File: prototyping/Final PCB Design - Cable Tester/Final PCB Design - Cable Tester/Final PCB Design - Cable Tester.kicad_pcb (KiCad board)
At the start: 2 copper layers, 86 x 54 mm, 41 parts, among them J17 Banana Jack, J20 SFML-110-02-L-D-A, J3 Debug Connection, J4 MicroSD, J5 Barrel Jack 9V, J6 Touchscreen HMI, Q1 2N3904, SW1 Rocker Switch, U1 AVR128DB64x-xMR, U2 LP2985-3.3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

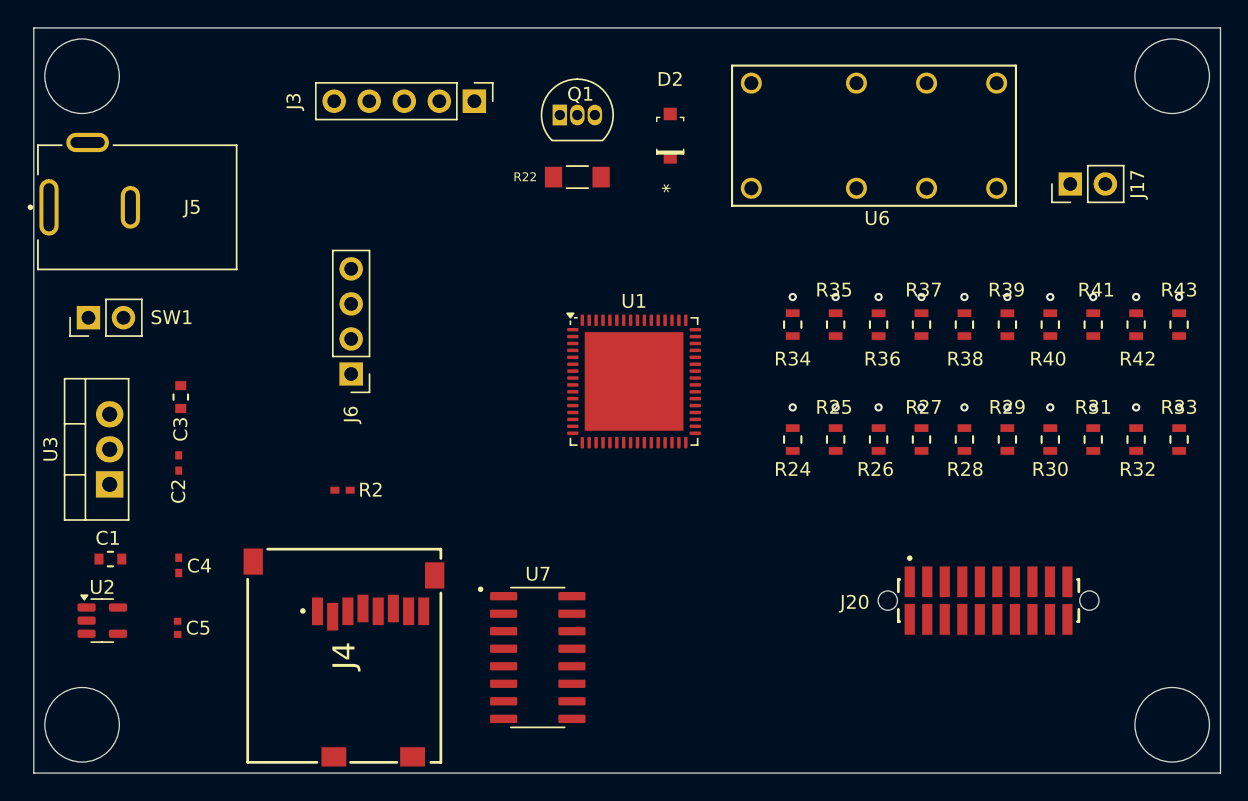
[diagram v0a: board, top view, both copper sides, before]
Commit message: Laying out final PCB.
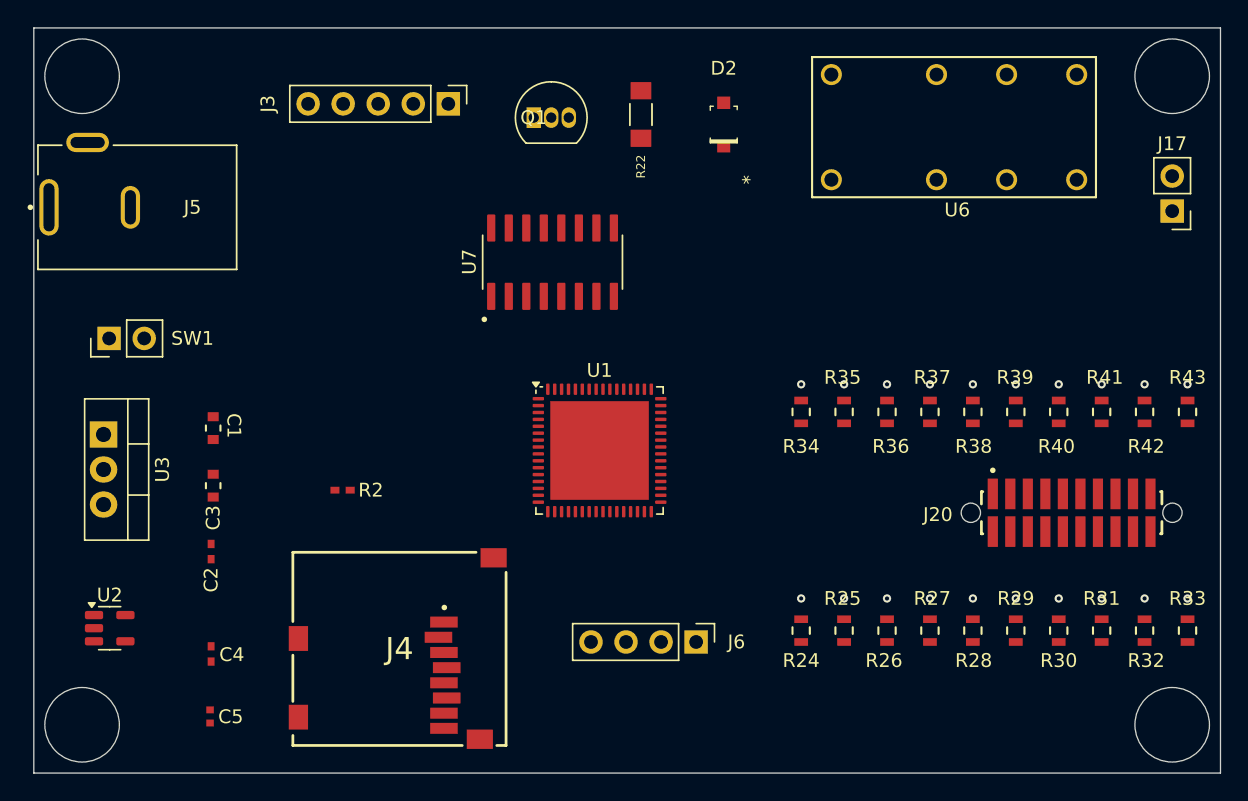
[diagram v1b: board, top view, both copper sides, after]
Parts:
- moved J6 31.7 mm to (139.5, 110.5), turned to -90 degrees
- moved U7 28.7 mm to (129.1, 83.0), turned to 90 degrees
- moved R24 13.9 mm to (147.1, 109.7)
- moved R25 13.9 mm to (150.2, 109.7)
- moved R26 13.9 mm to (153.3, 109.7)
- moved R27 13.9 mm to (156.4, 109.7)
- moved R28 13.9 mm to (159.6, 109.7)
- moved R29 13.9 mm to (162.7, 109.7)
- moved R30 13.9 mm to (165.8, 109.7)
- moved R31 13.9 mm to (168.9, 109.7)
- moved R32 13.9 mm to (172.0, 109.7)
- moved R33 13.9 mm to (175.1, 109.7)
- moved C1 12.1 mm to (104.5, 95.0), turned to -90 degrees
- moved J20 8.76 mm to (166.7, 101.1)
- moved J17 7.64 mm to (174.0, 79.3), turned to 180 degrees
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
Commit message: Updated.
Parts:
- moved U7 9.75 mm to (119.5, 81.1), turned to 180 degrees
- moved U1 2.85 mm to (135.1, 95.5)
- moved C1 1.00 mm to (104.5, 94.0), turned to 90 degrees

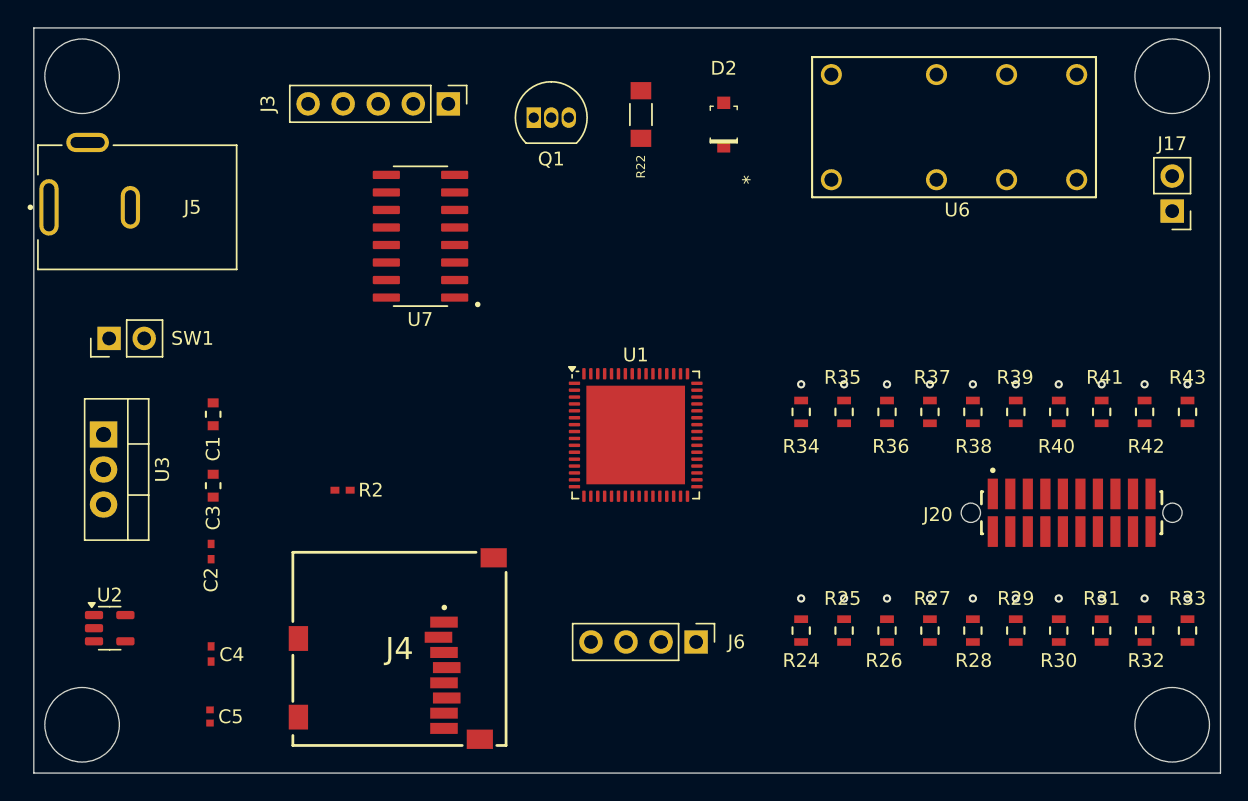
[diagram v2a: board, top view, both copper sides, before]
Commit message: Updates to final PCB
Final PCB design updates - placed traces and vias to Analog IF circuit and changed order of analog pins 1-10 on schematic and PCB layout.
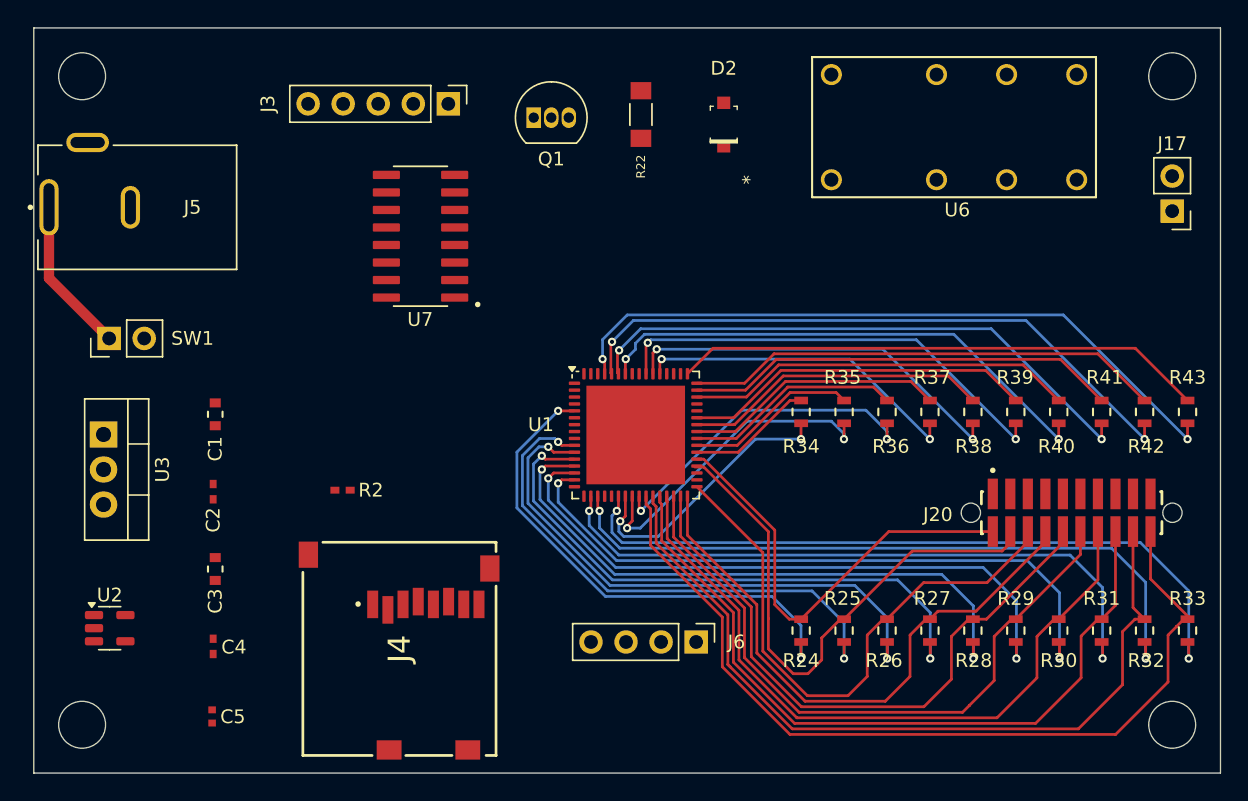
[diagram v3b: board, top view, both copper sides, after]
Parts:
- J4: value MicroSD -> MEM2061-01-188-00-A_REVA
- moved C3 6.04 mm to (104.7, 105.2)
- moved C2 4.34 mm to (104.5, 99.6)
- moved C4 0.57 mm to (104.5, 110.8)
- moved C1 0.15 mm to (104.7, 94.0)
- moved C5 0.15 mm to (104.4, 115.9)
- turned J4 to 180 degrees
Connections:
- C1 pad 2: CD -> GND
- C2 pad 2: CD -> GND
- C3 pad 2: CD -> GND
- C4 pad 2: CD -> GND
- C5 pad 2: CD -> GND
- J3 pad 1: CD -> GND
- J4 pad 11: CD -> GND
- J4 pad 12: CD -> GND
- J4 pad 2: CD -> /mSD_CS
- J4 pad 3: CD -> /mSD_DI
- J4 pad 5: CD -> /mSD_CLK
- J4 pad 6: CD -> GND
- J4 pad 7: CD -> /mSD_DO
- J5 pad B: CD -> GND
- J5 pad C: CD -> GND
- J6 pad 4: CD -> GND
- Q1 pad 1: CD -> GND
- U1 pad 21: CD -> GND
- U1 pad 26: ADC 1 -> ADC 10
- U1 pad 27: ADC 2 -> ADC 9
- U1 pad 28: ADC 3 -> ADC 8
- U1 pad 29: ADC 4 -> ADC 7
- U1 pad 30: ADC 5 -> ADC 6
- U1 pad 31: ADC 6 -> ADC 5
- U1 pad 32: ADC 7 -> ADC 4
- U1 pad 33: ADC 8 -> ADC 3
- U1 pad 35: CD -> GND
- U1 pad 36: ADC 9 -> ADC 2
- U1 pad 37: ADC 10 -> ADC 1
- U1 pad 57: CD -> GND
- U1 pad 65: CD -> GND
- U1 pad 7: CD -> GND
- U2 pad 2: CD -> GND
- U3 pad 2: CD -> GND
- U6 pad 4: CD -> GND
- U7 pad 10: CD -> /mSD_CLK
- U7 pad 11: CD -> GND
- U7 pad 14: CD -> GND
- U7 pad 2: CD -> /mSD_DO
- U7 pad 4: CD -> /mSD_CS
- U7 pad 6: CD -> /mSD_DI
- U7 pad 8: CD -> GND
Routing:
- net ADC 10: track 0.00 -> 63.3 mm
- net ADC 9: track 0.00 -> 59.1 mm
- net ADC 8: track 0.00 -> 54.4 mm
- net CTRL 10: track 0.00 -> 52.5 mm, vias 0 -> 2
- net ADC 7: track 0.00 -> 51.2 mm
- net CTRL 20: track 0.00 -> 50.5 mm, vias 0 -> 2
- net CTRL 9: track 0.00 -> 50.3 mm, vias 0 -> 2
- net ADC 6: track 0.00 -> 48.1 mm
- net CTRL 7: track 0.00 -> 47.7 mm, vias 0 -> 2
- net CTRL 8: track 0.00 -> 47.6 mm, vias 0 -> 2
- net CTRL 19: track 0.00 -> 46.3 mm, vias 0 -> 2
- net CTRL 6: track 0.00 -> 46.0 mm, vias 0 -> 2
- net ADC 5: track 0.00 -> 45.4 mm
- net CTRL 5: track 0.00 -> 44.3 mm, vias 0 -> 2
- net ADC 4: track 0.00 -> 43.1 mm
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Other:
- outline, holes or cut-outs redrawn

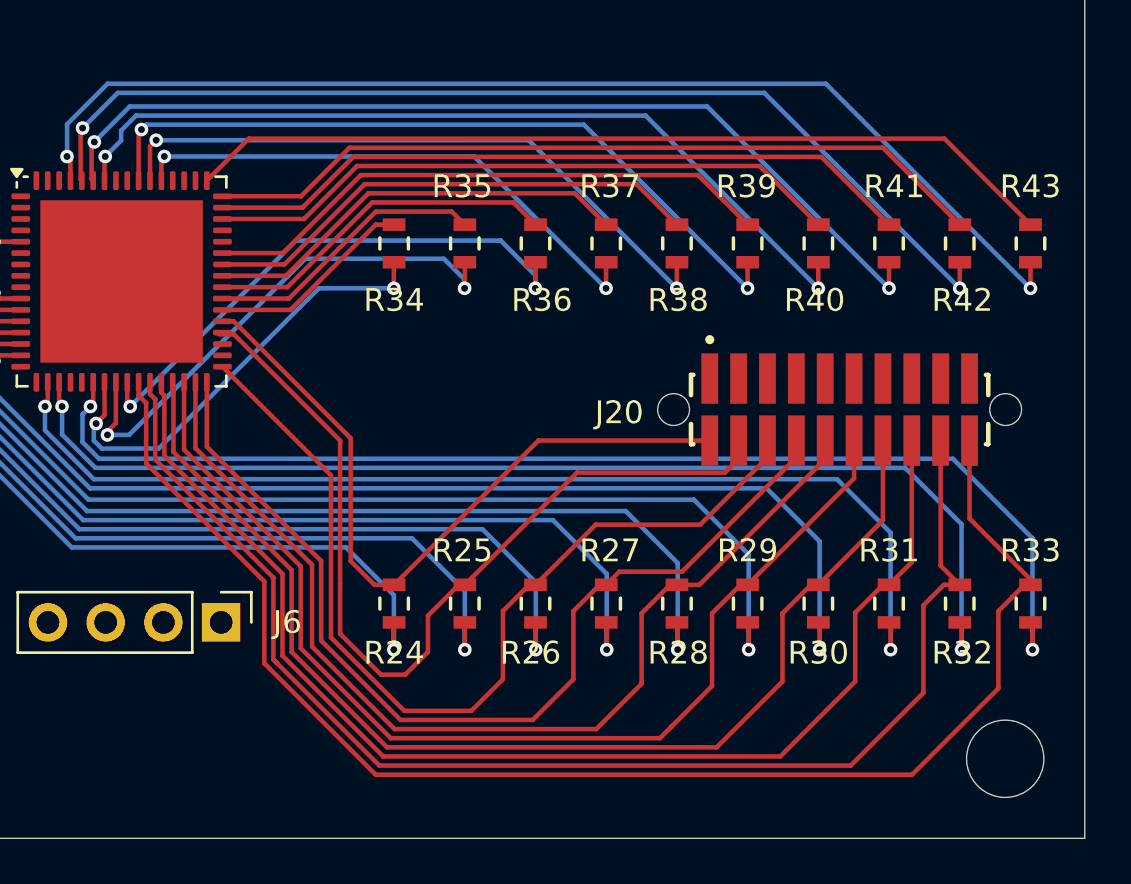
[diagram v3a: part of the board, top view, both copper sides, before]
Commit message: Updated Final PCB Layout
Refined some of the ADC trace layouts. Less sharp corners and smoother traces
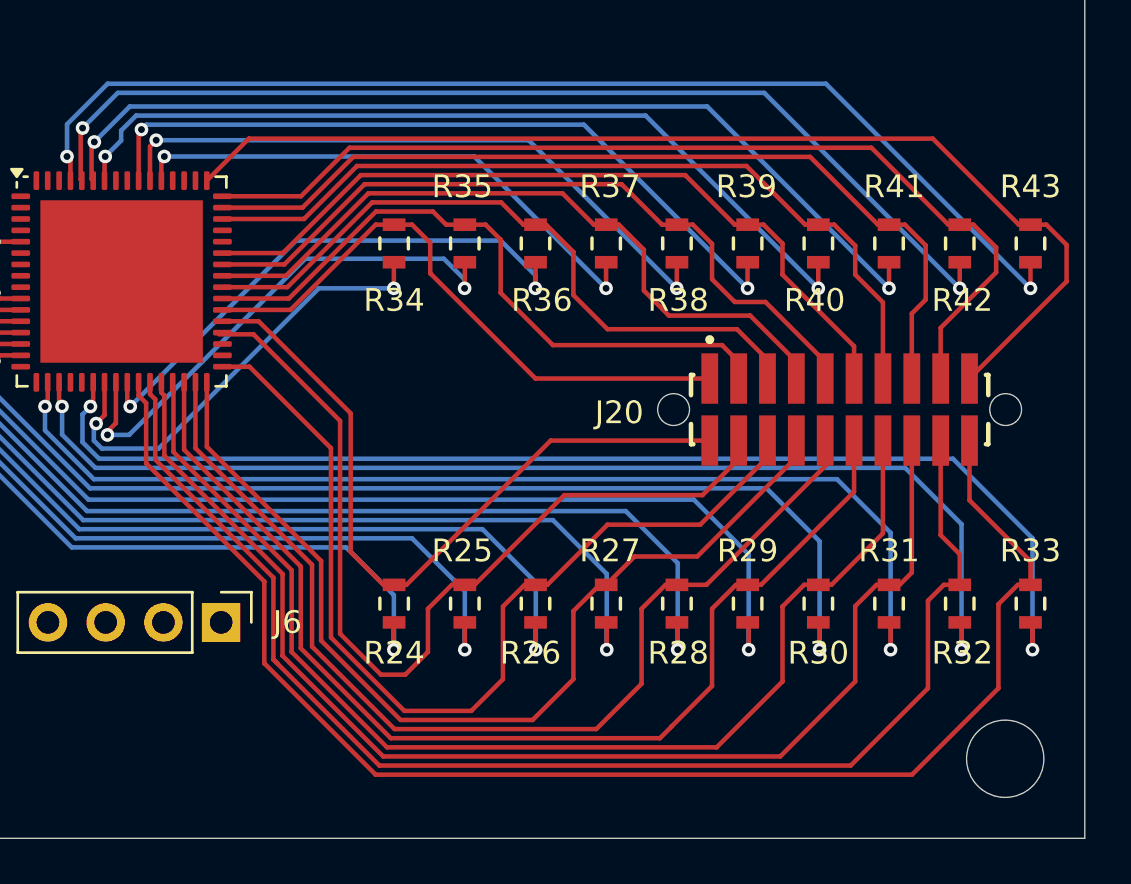
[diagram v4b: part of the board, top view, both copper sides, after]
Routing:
- net ADC 11: track 9.11 -> 26.6 mm
- net ADC 12: track 12.5 -> 29.1 mm
- net ADC 13: track 15.7 -> 30.3 mm
- net ADC 14: track 19.0 -> 31.6 mm
- net ADC 15: track 22.2 -> 32.9 mm
- net ADC 20: track 38.6 -> 48.2 mm
- net ADC 16: track 25.4 -> 34.6 mm
- net ADC 19: track 34.7 -> 43.5 mm
- net ADC 17: track 28.3 -> 36.6 mm
- net ADC 18: track 31.5 -> 39.6 mm
- net ADC 3: track 41.6 -> 42.4 mm
- net ADC 2: track 39.7 -> 40.4 mm
- net ADC 7: track 51.2 -> 51.7 mm

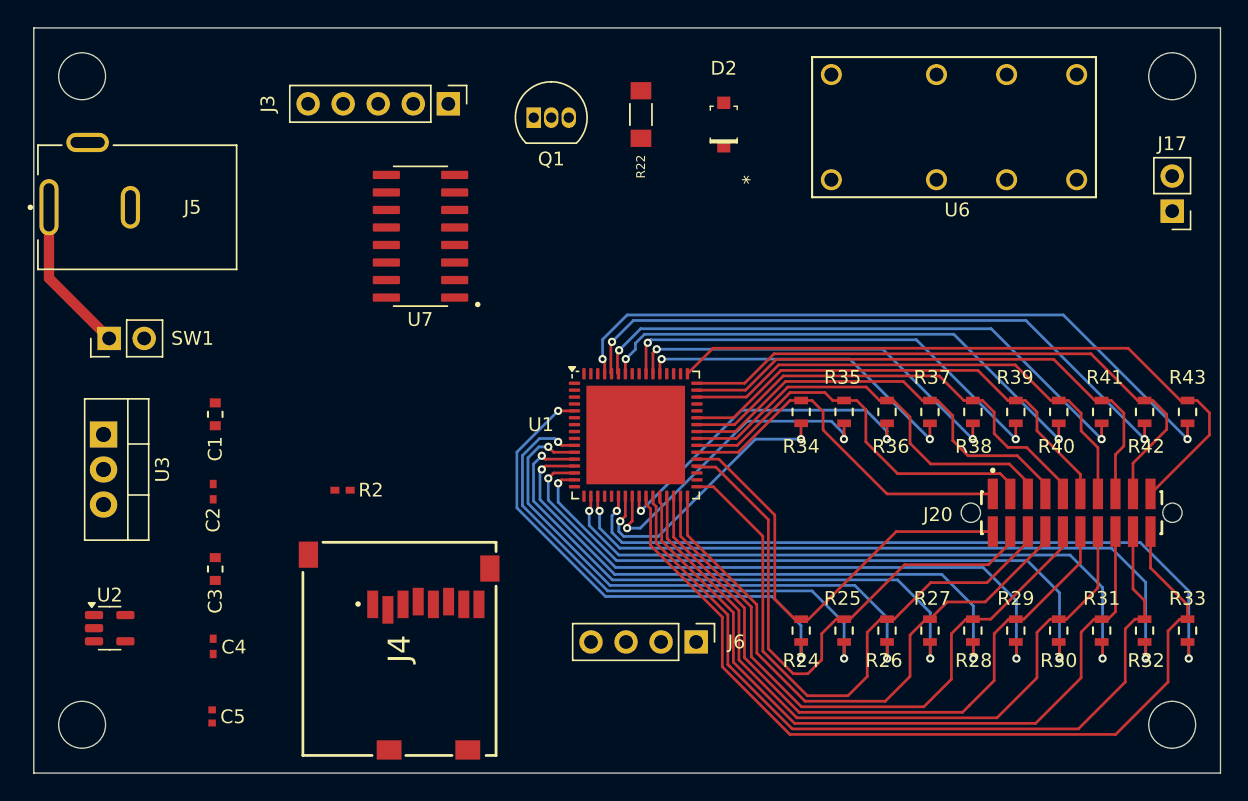
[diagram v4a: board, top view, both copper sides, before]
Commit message: updated prototype PCB layout
Fixed backwards barrel jack and made small minor changes to silkscreen layer so that paint is not overlapping solder points.
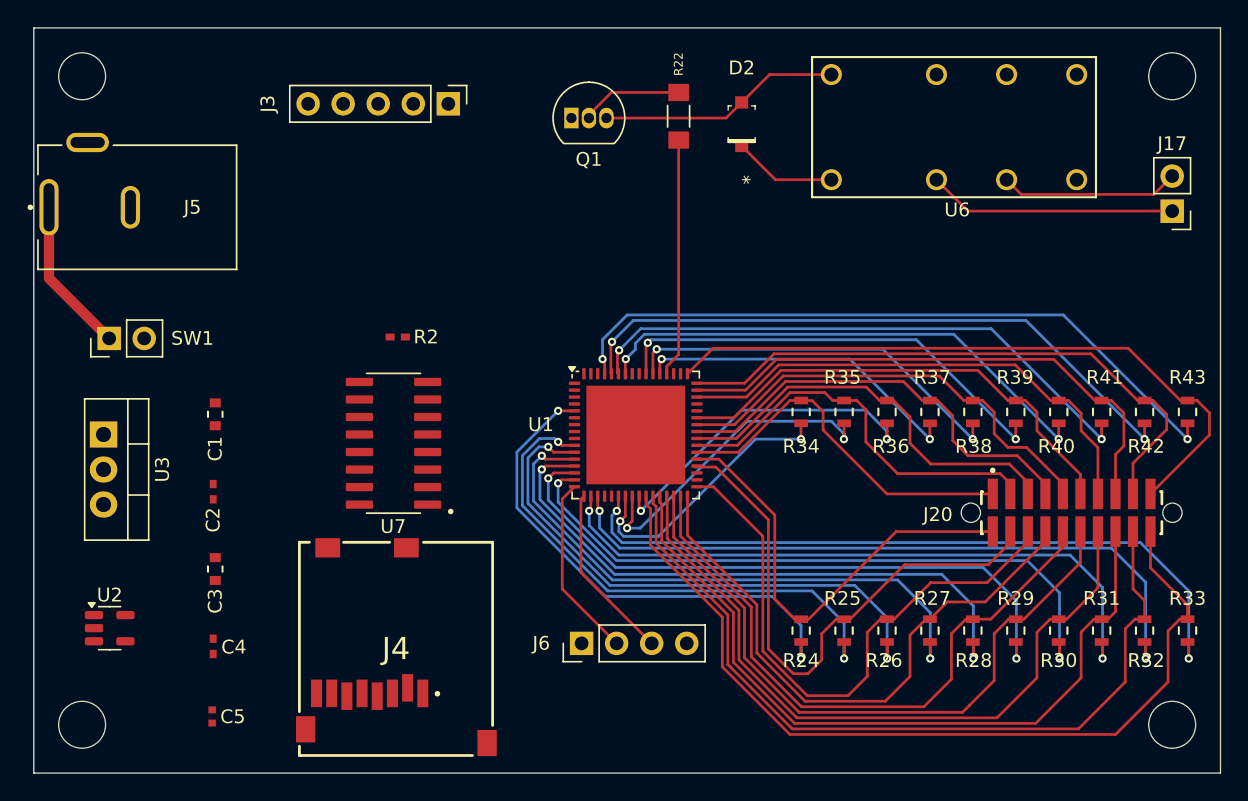
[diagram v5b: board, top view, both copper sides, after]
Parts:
- moved U7 15.1 mm to (117.6, 96.1)
- moved R2 11.8 mm to (117.9, 88.4)
- moved J6 8.30 mm to (131.2, 110.6), turned to 90 degrees
- moved R22 2.73 mm to (138.2, 72.4), turned to 90 degrees
- moved Q1 2.73 mm to (130.5, 72.5)
- moved D2 1.30 mm to (142.8, 73.0)
- moved J4 0.25 mm to (117.8, 111.0), turned to 0 degrees
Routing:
- net Net-(J17-Pin_1): track 0.00 -> 18.0 mm
- net Net-(Q1-C): track 0.00 -> 17.6 mm
- net RSig: track 0.00 -> 17.3 mm
- net Tx1: track 0.00 -> 13.3 mm
- net Net-(J17-Pin_2): track 0.00 -> 13.0 mm
- net Rx1: track 0.00 -> 12.9 mm
- net +5V: track 0.00 -> 7.51 mm
- net Net-(Q1-B): track 0.00 -> 7.40 mm
